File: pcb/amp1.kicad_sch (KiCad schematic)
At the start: 14 parts, among them Q1 BFP640, U1 Single_Stub_Input, U2 Single_Stub_Output

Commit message: Started PCB Layout
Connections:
- net RF1_IN_AM: now also L1.2, L2.2, Q1.1, U1.2
- net RF1_IN_BM: no longer L1.1, L2.2
- net DC1_2: now reaches C2.1, R3.1
- net DC1_2: now also L1.1; no longer L1.2
- net DC1_3: now reaches C3.1, L2.1, R1.1
- net DC1 renamed DC1_1
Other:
- moved on the sheet: L1
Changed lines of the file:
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@@
   (junction (at 153.67 88.9) (diameter 0) (color 0 0 0 0)
   )
+  (junction (at 153.67 99.06) (diameter 0) (color 0 0 0 0)
+  )
+  (junction (at 154.94 114.3) (diameter 0) (color 0 0 0 0)
+  )
+  (junction (at 146.05 106.68) (diameter 0) (color 0 0 0 0)
+  )
+  (junction (at 118.11 118.11) (diameter 0) (color 0 0 0 0)
+  )
   (junction (at 118.11 88.9) (diameter 0) (color 0 0 0 0)
   )
-  (junction (at 153.67 99.06) (diameter 0) (color 0 0 0 0)
-  )
-  (junction (at 154.94 114.3) (diameter 0) (color 0 0 0 0)
-  )
-  (junction (at 118.11 118.11) (diameter 0) (color 0 0 0 0)
-  )
-  (junction (at 118.11 106.68) (diameter 0) (color 0 0 0 0)
-  )
   (wire (pts (xy 153.67 97.79) (xy 153.67 99.06))
     (stroke (width 0) (type default) (color 0 0 0 0))
@@
     (stroke (width 0) (type default) (color 0 0 0 0))
   )
+  (wire (pts (xy 118.11 88.9) (xy 118.11 93.98))
+    (stroke (width 0) (type default) (color 0 0 0 0))
+  )
   (wire (pts (xy 154.94 128.27) (xy 154.94 114.3))
     (stroke (width 0) (type default) (color 0 0 0 0))
@@
     (stroke (width 0) (type default) (color 0 0 0 0))
   )
+  (wire (pts (xy 146.05 101.6) (xy 146.05 106.68))
+    (stroke (width 0) (type default) (color 0 0 0 0))
+  )
+  (wire (pts (xy 118.11 101.6) (xy 146.05 101.6))
+    (stroke (width 0) (type default) (color 0 0 0 0))
+  )
   (wire (pts (xy 153.67 99.06) (xy 161.29 99.06))
     (stroke (width 0) (type default) (color 0 0 0 0))
@@
     (stroke (width 0) (type default) (color 0 0 0 0))
   )
-  (wire (pts (xy 118.11 88.9) (xy 118.11 93.98))
-    (stroke (width 0) (type default) (color 0 0 0 0))
-  )
   (polyline (pts (xy 104.14 107.95) (xy 104.14 133.35))
     (stroke (width 0) (type default) (color 0 0 0 0))
   )
-  (wire (pts (xy 118.11 106.68) (xy 128.27 106.68))
+  (wire (pts (xy 107.95 106.68) (xy 128.27 106.68))
+    (stroke (width 0) (type default) (color 0 0 0 0))
+  )
+  (wire (pts (xy 146.05 106.68) (xy 148.59 106.68))
     (stroke (width 0) (type default) (color 0 0 0 0))
   )
@@
     (stroke (width 0) (type default) (color 0 0 0 0))
   )
-  (wire (pts (xy 143.51 106.68) (xy 148.59 106.68))
+  (wire (pts (xy 143.51 106.68) (xy 146.05 106.68))
     (stroke (width 0) (type default) (color 0 0 0 0))
   )
@@
     (stroke (width 0) (type default) (color 0 0 0 0))
   )
-  (wire (pts (xy 118.11 106.68) (xy 118.11 109.22))
-    (stroke (width 0) (type default) (color 0 0 0 0))
-  )
   (wire (pts (xy 111.76 90.17) (xy 111.76 88.9))
     (stroke (width 0) (type default) (color 0 0 0 0))
   )
-  (wire (pts (xy 107.95 106.68) (xy 118.11 106.68))
-    (stroke (width 0) (type default) (color 0 0 0 0))
-  )
-  (wire (pts (xy 118.11 101.6) (xy 118.11 106.68))
-    (stroke (width 0) (type default) (color 0 0 0 0))
-  )
   (wire (pts (xy 176.53 99.06) (xy 190.5 99.06))
     (stroke (width 0) (type default) (color 0 0 0 0))
   )
+  (polyline (pts (xy 127 107.95) (xy 127 133.35))
+    (stroke (width 0) (type default) (color 0 0 0 0))
+  )
+  (wire (pts (xy 118.11 127) (xy 118.11 128.27))
+    (stroke (width 0) (type default) (color 0 0 0 0))
+  )
+  (wire (pts (xy 146.05 109.22) (xy 146.05 106.68))
+    (stroke (width 0) (type default) (color 0 0 0 0))
+  )
+  (wire (pts (xy 118.11 109.22) (xy 146.05 109.22))
+    (stroke (width 0) (type default) (color 0 0 0 0))
+  )
+  (wire (pts (xy 153.67 88.9) (xy 153.67 90.17))
+    (stroke (width 0) (type default) (color 0 0 0 0))
+  )
+  (wire (pts (xy 153.67 87.63) (xy 153.67 88.9))
+    (stroke (width 0) (type default) (color 0 0 0 0))
+  )
+  (wire (pts (xy 153.67 99.06) (xy 153.67 100.33))
+    (stroke (width 0) (type default) (color 0 0 0 0))
+  )
+  (wire (pts (xy 153.67 88.9) (xy 161.29 88.9))
+    (stroke (width 0) (type default) (color 0 0 0 0))
+  )
   (wire (pts (xy 118.11 88.9) (xy 143.51 88.9))
-    (stroke (width 0) (type default) (color 0 0 0 0))
-  )
-  (polyline (pts (xy 127 107.95) (xy 127 133.35))
-    (stroke (width 0) (type default) (color 0 0 0 0))
-  )
-  (wire (pts (xy 118.11 127) (xy 118.11 128.27))
-    (stroke (width 0) (type default) (color 0 0 0 0))
-  )
-  (wire (pts (xy 153.67 88.9) (xy 153.67 90.17))
-    (stroke (width 0) (type default) (color 0 0 0 0))
-  )
-  (wire (pts (xy 153.67 87.63) (xy 153.67 88.9))
-    (stroke (width 0) (type default) (color 0 0 0 0))
-  )
-  (wire (pts (xy 153.67 99.06) (xy 153.67 100.33))
-    (stroke (width 0) (type default) (color 0 0 0 0))
-  )
-  (wire (pts (xy 153.67 88.9) (xy 161.29 88.9))
     (stroke (width 0) (type default) (color 0 0 0 0))
   )
@@
     (effects (font (size 1.27 1.27)) (justify left bottom))
   )
-  (label "DC1" (at 156.21 88.9 0)
-    (effects (font (size 1.27 1.27)) (justify left bottom))
-  )
-  (label "DC3" (at 120.65 119.38 0)
+  (label "DC1_1" (at 156.21 88.9 0)
+    (effects (font (size 1.27 1.27)) (justify left bottom))
+  )
+  (label "DC1_3" (at 118.11 118.11 0)
     (effects (font (size 1.27 1.27)) (justify left bottom))
   )
@@
     (effects (font (size 1.27 1.27)) (justify left bottom))
   )
-  (label "RF1_IN_AM" (at 143.51 107.95 0)
-    (effects (font (size 1.27 1.27)) (justify left bottom))
-  )
-  (label "DC2" (at 121.92 87.63 0)
+  (label "RF1_IN_AM" (at 144.78 106.68 0)
+    (effects (font (size 1.27 1.27)) (justify left bottom))
+  )
+  (label "DC1_2" (at 116.84 88.9 0)
     (effects (font (size 1.27 1.27)) (justify left bottom))
   )
@@
     (pin "2")
   )
-  (symbol (lib_id "Device:L") (at 118.11 97.79 180) (unit 1)
+  (symbol (lib_id "Device:L") (at 118.11 97.79 0) (unit 1)
     (in_bom yes) (on_board yes) (fields_autoplaced)
     (property "Reference" "L1" (id 0) (at 119.38 96.5199 0)
-      (effects (font (size 1.27 1.27)) (justify right))
+      (effects (font (size 1.27 1.27)) (justify left))
     )
     (property "Value" "7.15nH" (id 1) (at 119.38 99.0599 0)
-      (effects (font (size 1.27 1.27)) (justify right))
+      (effects (font (size 1.27 1.27)) (justify left))
     )
     (property "Footprint" "Nicobigio01:Coilcraft_1606-xxLx" (id 2) (at 118.11 97.79 0)

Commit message: backup version before changes
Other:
- moved on the sheet: C3, L1, L2, R1

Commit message: backup version before changes
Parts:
- added C?: 100nF, Capacitor_SMD:C_1206_3216Metric, symbol Device:C
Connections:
- net GND: now also C?.2
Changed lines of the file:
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@@
+    (stroke (width 0) (type default) (color 0 0 0 0))
+  )
+  (wire (pts (xy 59.69 109.22) (xy 59.69 110.49))
     (stroke (width 0) (type default) (color 0 0 0 0))
   )
@@
   )
   (wire (pts (xy 153.67 77.47) (xy 153.67 80.01))
+    (stroke (width 0) (type default) (color 0 0 0 0))
+  )
+  (wire (pts (xy 59.69 101.6) (xy 59.69 100.33))
     (stroke (width 0) (type default) (color 0 0 0 0))
   )
@@
   (hierarchical_label "VCC" (shape input) (at 153.67 77.47 90)
     (effects (font (size 1.27 1.27)) (justify left))
+  )
+  (symbol (lib_id "Device:C") (at 59.69 105.41 0) (mirror y) (unit 1)
+    (in_bom yes) (on_board yes)
+    (property "Reference" "C?" (id 0) (at 52.07 100.33 0)
+      (effects (font (size 1.27 1.27)) (justify right))
+    )
+    (property "Value" "100nF" (id 1) (at 52.07 102.87 0)
+      (effects (font (size 1.27 1.27)) (justify right))
+    )
+    (property "Footprint" "Capacitor_SMD:C_1206_3216Metric" (id 2) (at 58.7248 109.22 0)
+      (effects (font (size 1.27 1.27)) hide)
+    )
+    (property "Datasheet" "~" (id 3) (at 59.69 105.41 0)
+      (effects (font (size 1.27 1.27)) hide)
+    )
+    (pin "1")
+    (pin "2")
   )
   (symbol (lib_id "Device:C") (at 111.76 93.98 0) (mirror y) (unit 1)
@@
     (pin "2")
   )
+  (symbol (lib_id "power:GND") (at 59.69 110.49 0) (unit 1)
+    (in_bom yes) (on_board yes) (fields_autoplaced)
+    (property "Reference" "#PWR?" (id 0) (at 59.69 116.84 0)
+      (effects (font (size 1.27 1.27)) hide)
+    )
+    (property "Value" "GND" (id 1) (at 59.69 115.57 0))
+    (property "Footprint" "" (id 2) (at 59.69 110.49 0)
+      (effects (font (size 1.27 1.27)) hide)
+    )
+    (property "Datasheet" "" (id 3) (at 59.69 110.49 0)
+      (effects (font (size 1.27 1.27)) hide)
+    )
+    (pin "1")
+  )
   (symbol (lib_id "power:GND") (at 111.76 99.06 0) (unit 1)

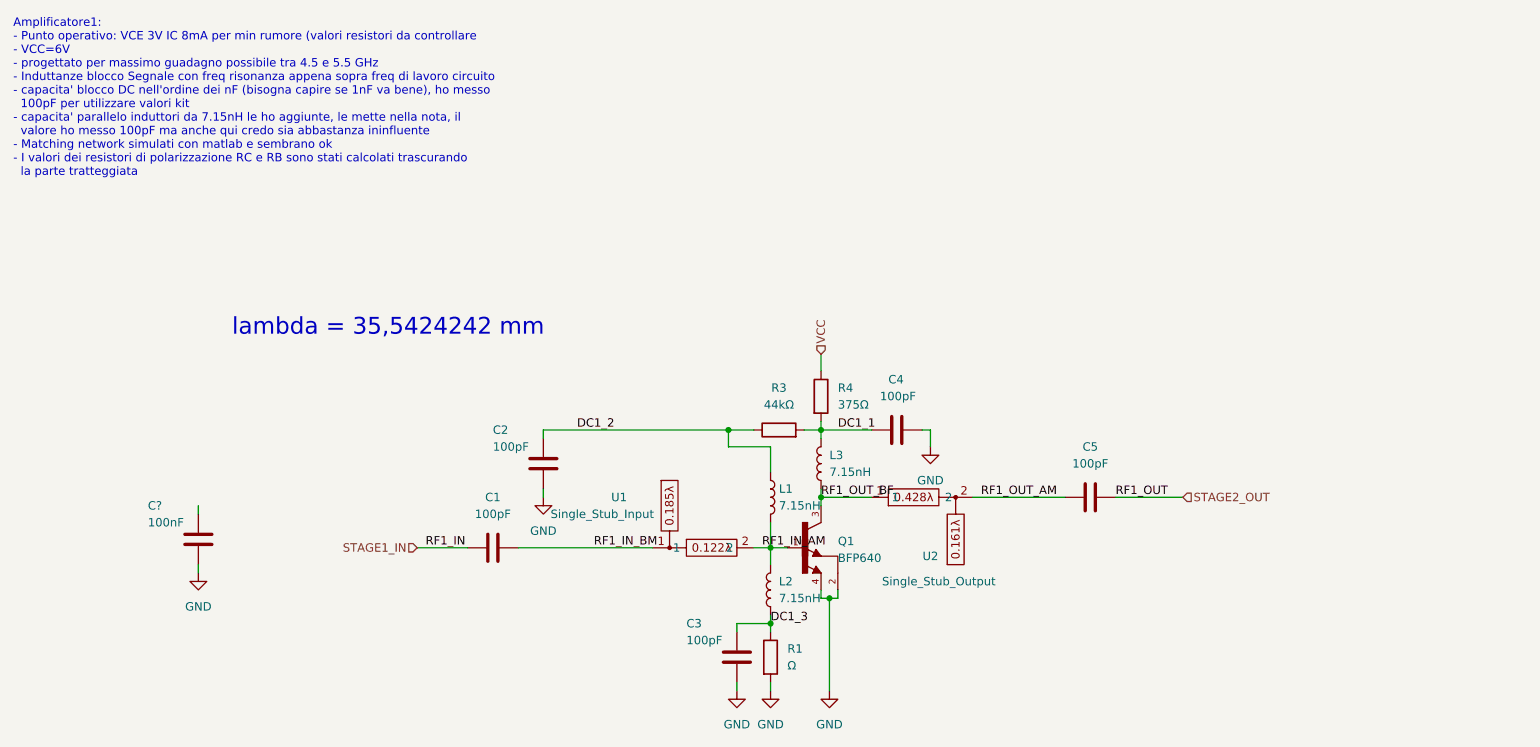
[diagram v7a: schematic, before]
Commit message: PCB modified according to suggestions
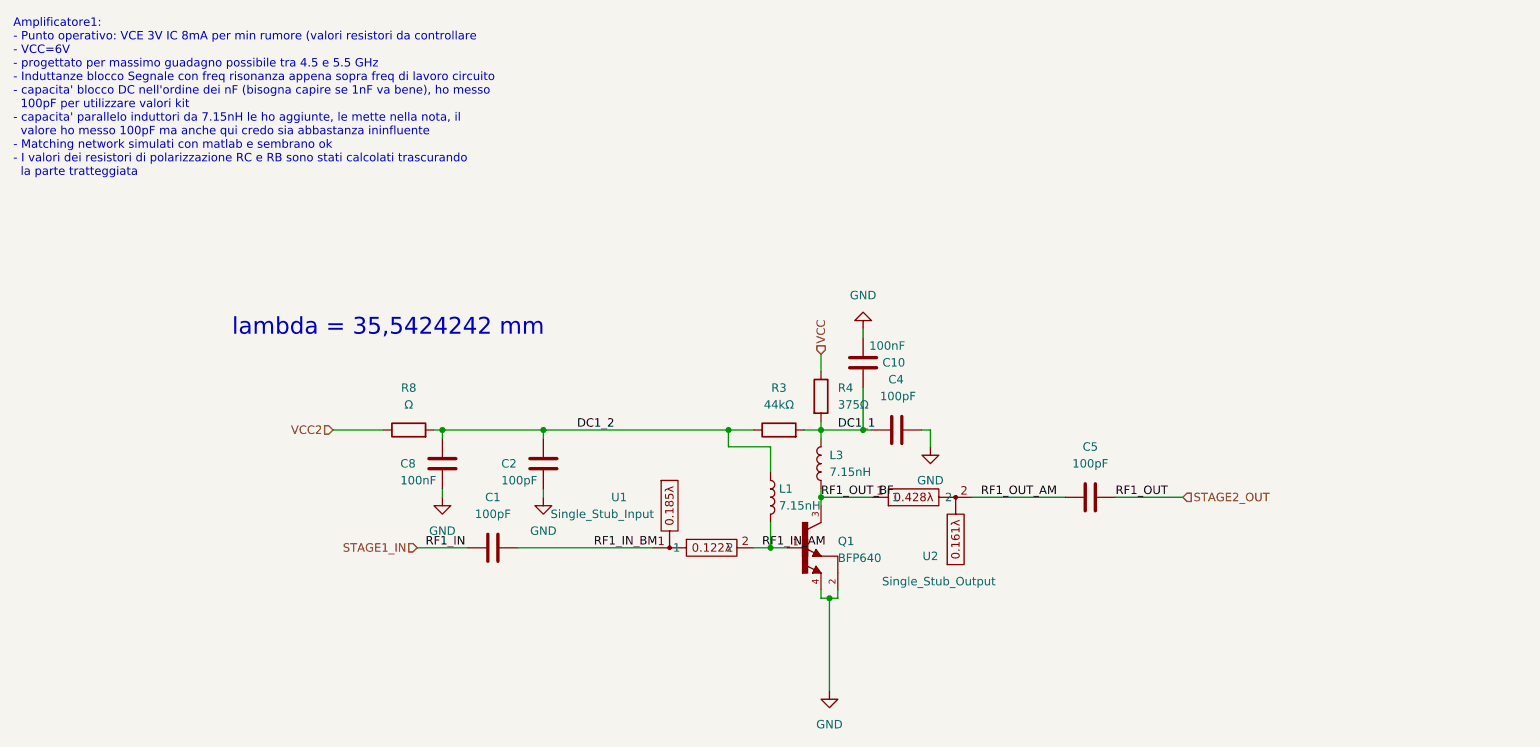
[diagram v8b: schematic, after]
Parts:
- removed C3: 100pF, Capacitor_SMD:C_0603_1608Metric, symbol Device:C
- removed L2: 7.15nH, Nicobigio01:Coilcraft_1606-xxLx, symbol Device:L
- removed R1: Ω, Resistor_SMD:R_0603_1608Metric, symbol Device:R
- added C10: 100nF, Capacitor_SMD:C_1206_3216Metric, symbol Device:C
- added R8: Ω, Resistor_SMD:R_0603_1608Metric, symbol Device:R
- gave numbers to parts that had none: 1
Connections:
- net DC1_1: now also C10.1
- net DC1_2: now also C8.1, R8.2
- net GND: now also C10.2
- new net VCC2: R8.1
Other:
- moved on the sheet: C8
